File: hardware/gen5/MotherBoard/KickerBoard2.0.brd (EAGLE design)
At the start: 143.9 x 141.8 mm, 155 parts

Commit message: almost done
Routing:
- net GND: track 273.4 -> 504.3 mm, vias 18 -> 23
- net KICK_ENABLE: track 2.64 -> 164.2 mm, vias 0 -> 4
- net BATSENSE: track 14.0 -> 171.4 mm, vias 1 -> 3
- net 12VGND: track 516.5 -> 661.6 mm, vias 15 -> 18
- net SCL-H: track 58.5 -> 153.0 mm, vias 3 -> 6
- net DRIB: track 2.34 -> 81.5 mm, vias 0 -> 1
- net CTS: track 0.00 -> 79.0 mm, vias 0 -> 1
- net ENABLE2: track 0.00 -> 77.4 mm, vias 0 -> 3
- net RTS: track 0.02 -> 63.1 mm, vias 0 -> 1
- net N$2: track 4.54 -> 66.4 mm, vias 2 -> 3
- net SDA-H: track 54.2 -> 109.8 mm, vias 4 -> 6
- net RX: track 3.24 -> 58.6 mm
- net TX: track 2.02 -> 55.5 mm
- net N$5: track 11.5 -> 57.9 mm
- net CHIP: track 24.5 -> 69.7 mm, vias 2 -> 4
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
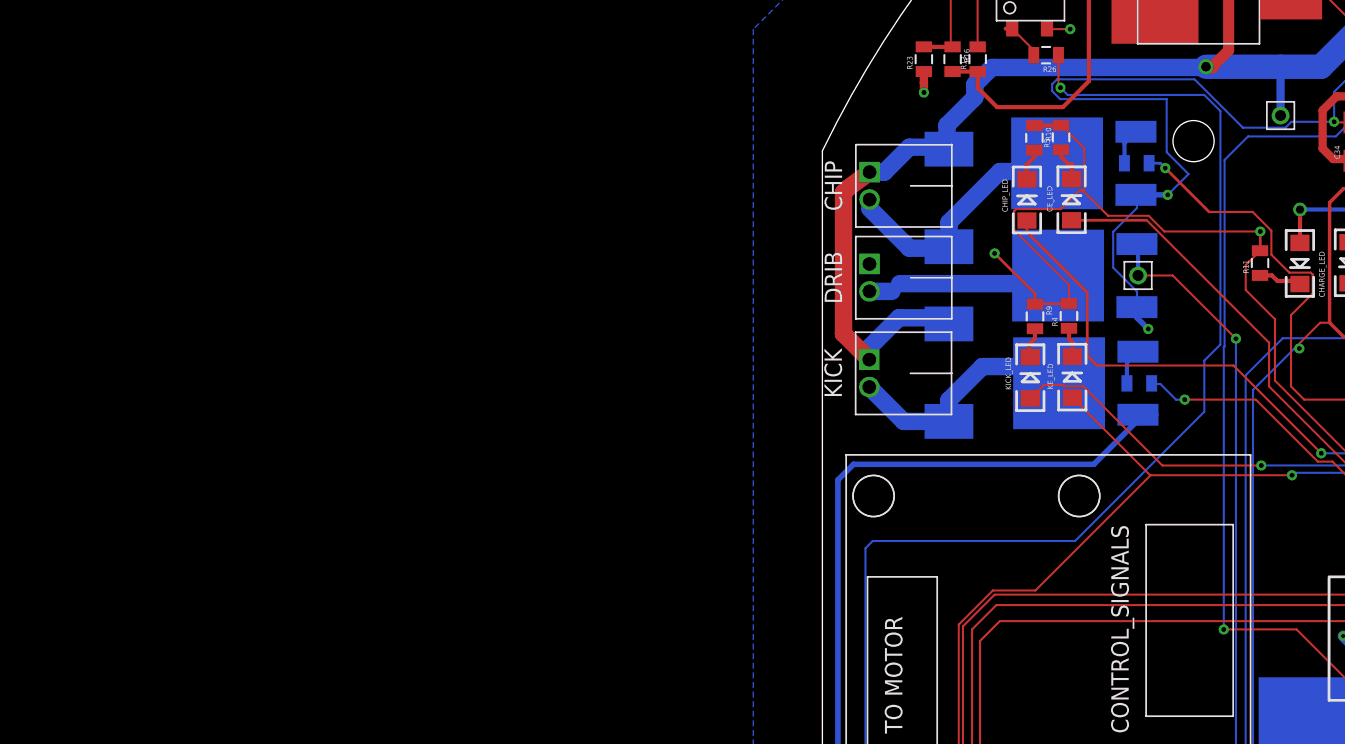
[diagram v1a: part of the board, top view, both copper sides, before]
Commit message: added big ol' transistors
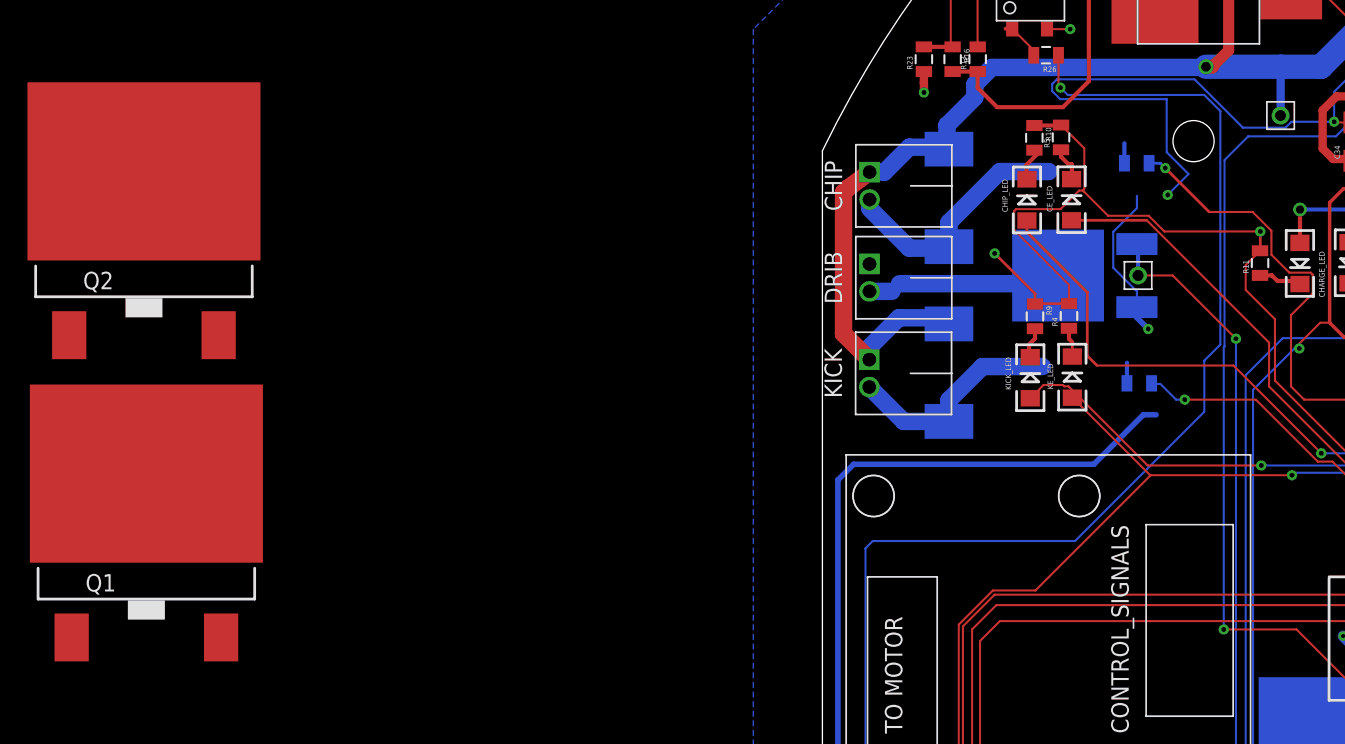
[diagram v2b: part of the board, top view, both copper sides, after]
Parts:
- removed KICK_Q, KICK_Q1: (no value), gen3:DPAK
- added Q1, Q2: IXGT6N170, transistor-power:TO268
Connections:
- net 12VGND: now also Q1.E, Q2.E; no longer KICK_Q.SOURCE, KICK_Q1.SOURCE
- net LOWCHIP: now also Q1.C@1, Q1.C@2; no longer KICK_Q1.DRAIN
- net LOWKICK: now also Q2.C@1, Q2.C@2; no longer KICK_Q.DRAIN
- net N$3: now also Q1.G; no longer KICK_Q1.GATE
- net N$8: now also Q2.G; no longer KICK_Q.GATE
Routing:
- net 12VGND: track 661.6 -> 658.8 mm
- net LOWKICK: track 18.0 -> 16.2 mm
- net N$3: track 2.64 -> 1.46 mm
- net N$8: track 2.64 -> 1.50 mm
- net LOWCHIP: track 19.1 -> 18.3 mm
